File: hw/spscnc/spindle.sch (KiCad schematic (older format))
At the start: 33 parts, among them J1 8P8C_4xShielded, J2 8P8C_4xShielded, J3 Conn_01x04_Female, Q1 KIA50N06B, Q2 KIA50N06B, Q3 KIA50N06B, Q4 KIA50N06B, U1 IR2104, U2 IR2104

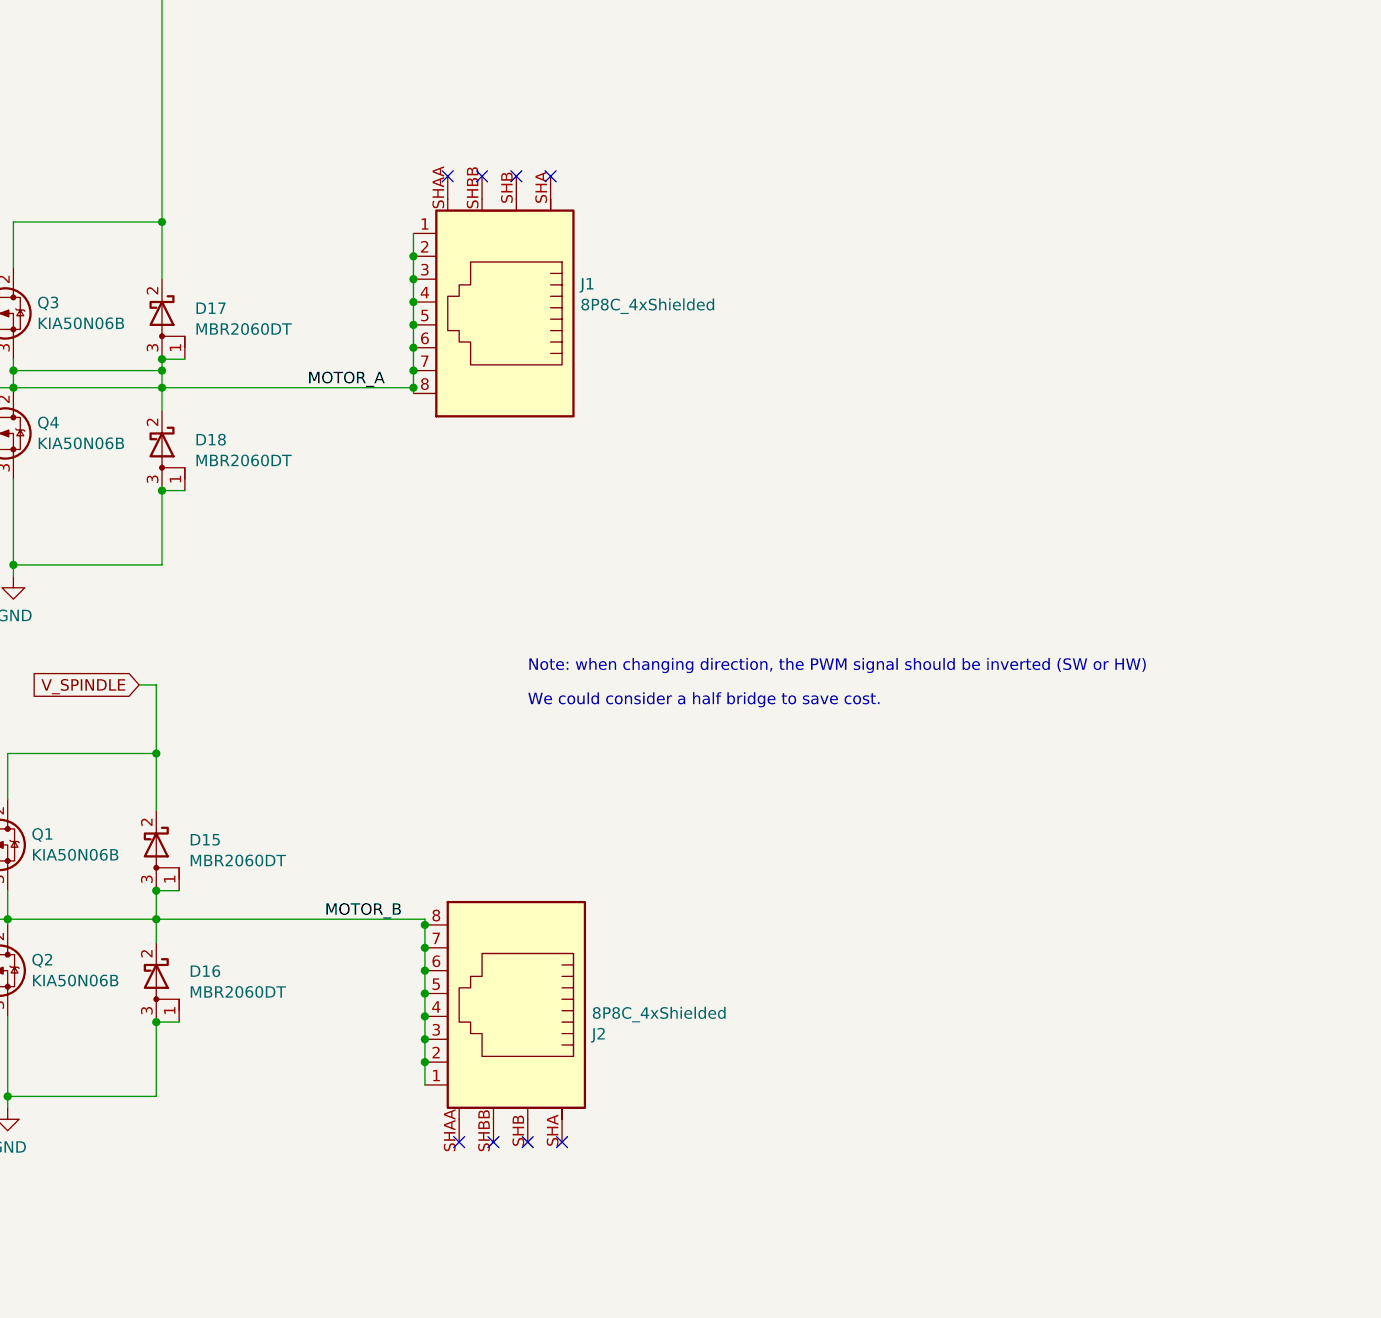
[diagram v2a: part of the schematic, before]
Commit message: added most corrections on the schematic for i2s operation.
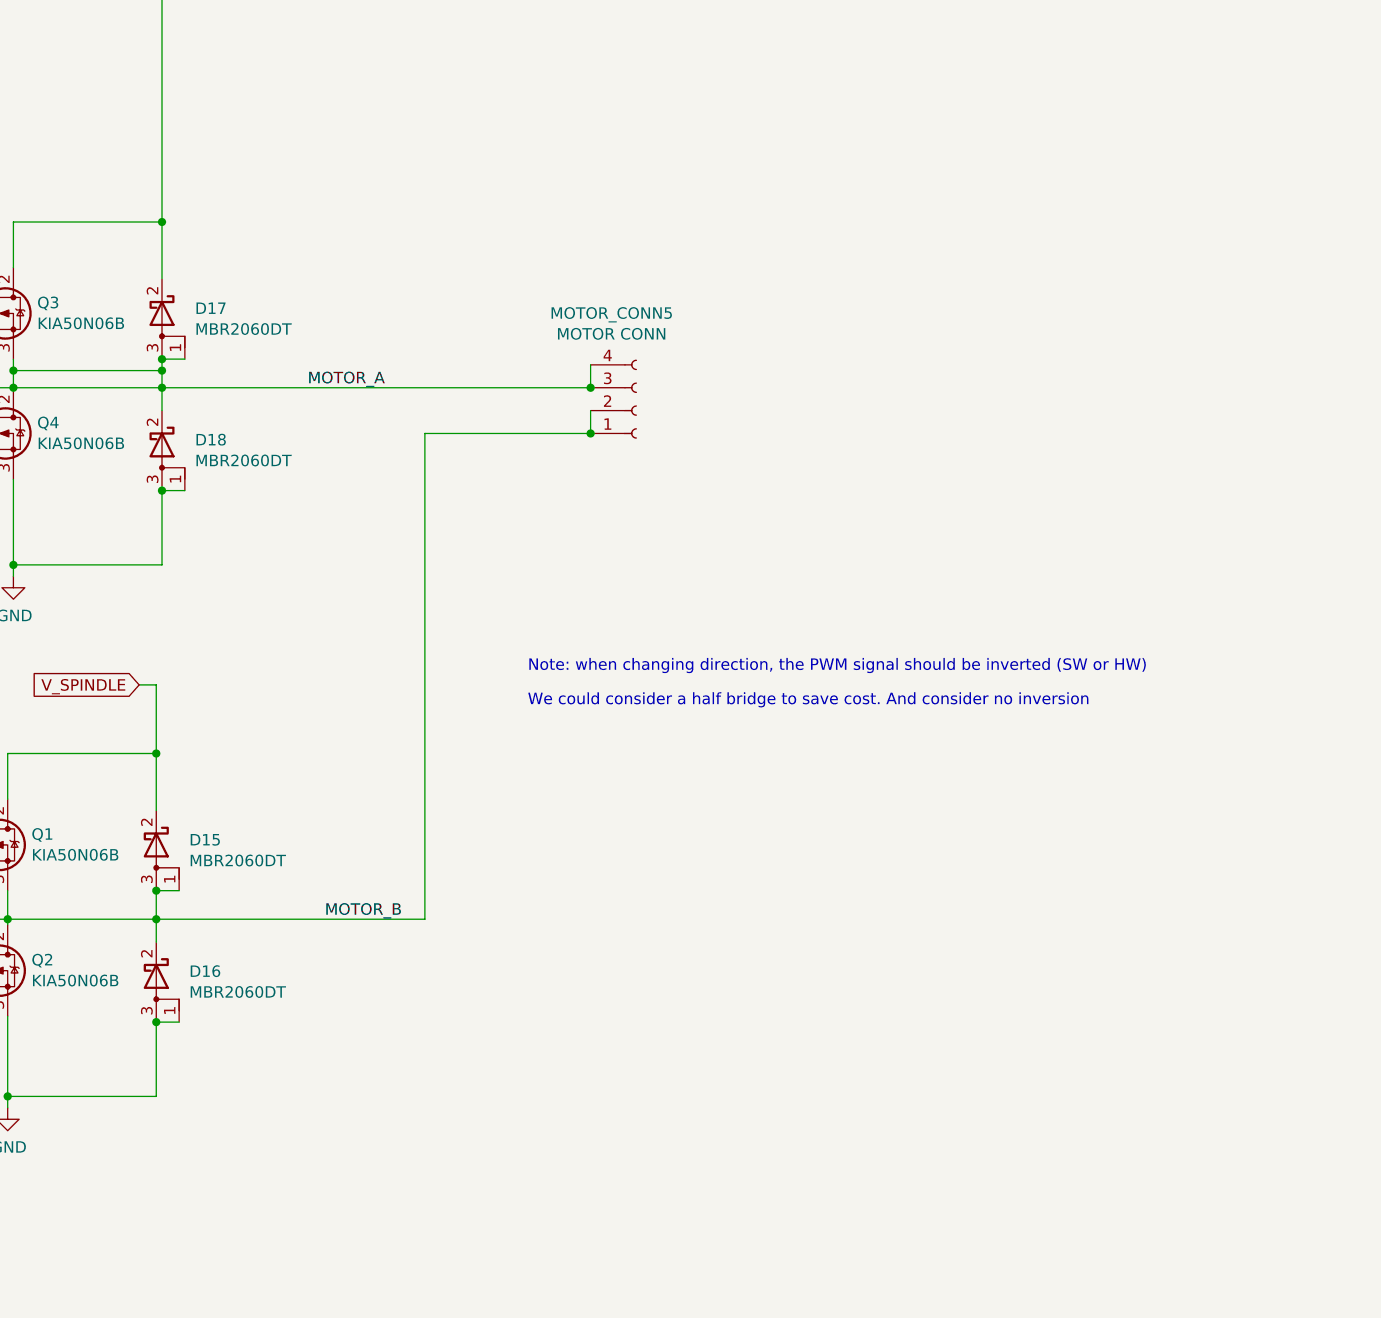
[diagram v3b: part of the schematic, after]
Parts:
- removed J1, J2: 8P8C_4xShielded, industrial000:rj45_R-RJ45S08P-B000_C386763, symbol industrial:8P8C_4xShielded
- added MOTOR_CONN5: MOTOR CONN, Connector_Phoenix_MSTB:PhoenixContact_MSTBV_2,5_4-GF-5,08_1x04_P5.08mm_Vertical_ThreadedFlange_MountHole, symbol Connector:Conn_01x04_Female
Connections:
- net MOTOR_A: now also MOTOR_CONN5.3 (Pin_3), MOTOR_CONN5.4 (Pin_4)
- net MOTOR_B: now also MOTOR_CONN5.1 (Pin_1), MOTOR_CONN5.2 (Pin_2)
- no-connect marks 8 -> 0
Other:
- note added: "We could consider a half bridge to save cost. And consider no inversion"
- note removed: "We could consider a half bridge to save cost."
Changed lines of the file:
@@
 $Descr A4 11693 8268
 encoding utf-8
-Sheet 5 16
+Sheet 5 17
 Title "Trinamic FluidNC CNC Controller"
 Date "2022-01-27"
@@
 Text HLabel 3575 2475 0    50   Input ~ 0
 PWM_IN
-NoConn ~ 7175 1750
-NoConn ~ 7325 1750
-NoConn ~ 7475 1750
-NoConn ~ 7625 1750
-NoConn ~ 7675 5975
-NoConn ~ 7525 5975
-NoConn ~ 7375 5975
-NoConn ~ 7225 5975
 Text Label 6900 2675 2    50   ~ 0
 MOTOR_A
-Wire Wire Line
-	7025 2700 7025 2675
-Connection ~ 7025 2600
-Wire Wire Line
-	7025 2600 7025 2500
-Connection ~ 7025 2500
-Wire Wire Line
-	7025 2500 7025 2400
-Connection ~ 7025 2400
-Wire Wire Line
-	7025 2400 7025 2300
-Connection ~ 7025 2300
-Wire Wire Line
-	7025 2300 7025 2200
-Connection ~ 7025 2200
-Wire Wire Line
-	7025 2200 7025 2100
-Connection ~ 7025 2100
-Wire Wire Line
-	7025 2100 7025 2000
-Wire Wire Line
-	7075 5725 7075 5625
-Connection ~ 7075 5025
-Connection ~ 7075 5125
-Wire Wire Line
-	7075 5125 7075 5025
-Connection ~ 7075 5225
-Wire Wire Line
-	7075 5225 7075 5125
-Connection ~ 7075 5325
-Wire Wire Line
-	7075 5325 7075 5225
-Connection ~ 7075 5425
-Wire Wire Line
-	7075 5425 7075 5325
-Connection ~ 7075 5525
-Wire Wire Line
-	7075 5525 7075 5425
-Connection ~ 7075 5625
-Wire Wire Line
-	7075 5625 7075 5525
 Text Label 6975 5000 2    50   ~ 0
 MOTOR_B
@@
 Wire Wire Line
 	5275 2675 5925 2675
-Connection ~ 7025 2675
-Wire Wire Line
-	7025 2675 7025 2600
 Connection ~ 5925 2675
 Wire Wire Line
 	5925 2675 5925 2600
 Wire Wire Line
-	5925 2675 7025 2675
-Wire Wire Line
 	5925 2675 5925 2775
 Wire Wire Line
 	5900 5000 7075 5000
-Wire Wire Line
-	7075 5000 7075 5025
 Wire Wire Line
 	5900 5000 5900 5100
@@
 Wire Wire Line
 	2725 1600 2725 1575
-$Comp
-L industrial:8P8C_4xShielded J?
-U 1 1 61D212C1
-P 7425 2300
-AR Path="/61C80DFB/61D212C1" Ref="J?"  Part="1"
-AR Path="/61C80E48/61D212C1" Ref="J?"  Part="1"
-AR Path="/61C80E8F/61D212C1" Ref="J?"  Part="1"
-AR Path="/61CEF4C9/61D212C1" Ref="J?"  Part="1"
-AR Path="/61C80DCB/61D212C1" Ref="J1"  Part="1"
-F 0 "J1" H 7095 2222 50  0000 R CNN
-F 1 "8P8C_4xShielded" H 7095 2313 50  0000 R CNN
-F 2 "industrial000:rj45_R-RJ45S08P-B000_C386763" V 7425 2325 50  0001 C CNN
-F 3 "~" V 7425 2325 50  0001 C CNN
-F 4 "DNP007" H 7425 2300 50  0001 C CNN "jlcpcb"
-	1    7425 2300
-	-1   0    0    1
-$EndComp
-$Comp
-L industrial:8P8C_4xShielded J?
-U 1 1 61D219D4
-P 7475 5425
-AR Path="/61C80DFB/61D219D4" Ref="J?"  Part="1"
-AR Path="/61C80E48/61D219D4" Ref="J?"  Part="1"
-AR Path="/61C80E8F/61D219D4" Ref="J?"  Part="1"
-AR Path="/61CEF4C9/61D219D4" Ref="J?"  Part="1"
-AR Path="/61C80DCB/61D219D4" Ref="J2"  Part="1"
-F 0 "J2" H 7145 5347 50  0000 R CNN
-F 1 "8P8C_4xShielded" H 7145 5438 50  0000 R CNN
-F 2 "industrial000:rj45_R-RJ45S08P-B000_C386763" V 7475 5450 50  0001 C CNN
-F 3 "~" V 7475 5450 50  0001 C CNN
-F 4 "DNP007" H 7475 5425 50  0001 C CNN "jlcpcb"
-	1    7475 5425
-	-1   0    0    -1
-$EndComp
 $Comp
 L Driver_FET:IR2104 U2
@@
 $EndComp
 Text Notes 7525 4075 0    50   ~ 0
-We could consider a half bridge to save cost.
+We could consider a half bridge to save cost. And consider no inversion
 $Comp
 L Device:R R150
@@
 Wire Wire Line
 	1475 6025 2200 6025
+$Comp
+L Connector:Conn_01x04_Female MOTOR_CONN?
+U 1 1 623B8ED3
+P 8000 2775
+AR Path="/61E0961E/623B8ED3" Ref="MOTOR_CONN?"  Part="1"
+AR Path="/61C743E7/61AF0AE8/623B8ED3" Ref="MOTOR_CONN?"  Part="1"
+AR Path="/61E601B6/623B8ED3" Ref="MOTOR_CONN?"  Part="1"
+AR Path="/6203D74D/623B8ED3" Ref="MOTOR_CONN?"  Part="1"
+AR Path="/6203DA5D/623B8ED3" Ref="MOTOR_CONN?"  Part="1"
+AR Path="/6203DFCF/623B8ED3" Ref="MOTOR_CONN?"  Part="1"
+AR Path="/6221509B/623B8ED3" Ref="MOTOR_CONN?"  Part="1"
+AR Path="/61C80DCB/623B8ED3" Ref="MOTOR_CONN5"  Part="1"
+F 0 "MOTOR_CONN5" H 7892 2350 50  0000 C CNN
+F 1 "MOTOR CONN" H 7892 2441 50  0000 C CNN
+F 2 "Connector_Phoenix_MSTB:PhoenixContact_MSTBV_2,5_4-GF-5,08_1x04_P5.08mm_Vertical_ThreadedFlange_MountHole" H 8000 2775 50  0001 C CNN
+F 3 "~" H 8000 2775 50  0001 C CNN
+F 4 "DNP006" H 8000 2775 50  0001 C CNN "jlcpcb"
+	1    8000 2775
+	1    0    0    1
+$EndComp
+Wire Wire Line
+	7800 2675 7800 2575
+Connection ~ 7800 2675
+Wire Wire Line
+	5925 2675 7800 2675
+Wire Wire Line
+	7800 2875 7800 2775
+Wire Wire Line
+	7800 2875 7075 2875
+Wire Wire Line
+	7075 2875 7075 5000
+Connection ~ 7800 2875
 $EndSCHEMATC

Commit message: Finished preliminary routing, pending checklist and review
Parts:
- removed C10: 330uF @60V, Capacitor_THT:CP_Radial_D24.0mm_P10.00mm_SnapIn, symbol Device:CP
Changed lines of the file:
@@
 	1525 1000 1525 875
 Connection ~ 1525 875
-Wire Wire Line
-	1525 875  1750 875
 $Comp
 L power:GND-power #PWR01
@@
 Wire Wire Line
 	1525 1425 1525 1300
-Wire Wire Line
-	1525 1300 1750 1300
 Connection ~ 1525 1300
-Connection ~ 1750 1300
-Wire Wire Line
-	1750 1300 2175 1300
 Wire Wire Line
 	2175 1000 2175 875
@@
 Wire Wire Line
 	2175 875  5925 875
-Wire Wire Line
-	1750 1000 1750 875
-Connection ~ 1750 875
-Wire Wire Line
-	1750 875  2175 875
 Wire Wire Line
 	2950 1600 2725 1600
@@
 	1    5900 5250
 	0    1    1    0
-$EndComp
-$Comp
-L Device:CP C10
-U 1 1 61E7AF08
-P 1750 1150
-F 0 "C10" H 1775 1250 50  0000 L CNN
-F 1 "330uF @60V" H 1750 900 50  0000 L CNN
-F 2 "Capacitor_THT:CP_Radial_D24.0mm_P10.00mm_SnapIn" H 1788 1000 50  0001 C CNN
-F 3 "~" H 1750 1150 50  0001 C CNN
-F 4 "DNP015" H 1750 1150 50  0001 C CNN "jlcpcb"
-	1    1750 1150
-	1    0    0    -1
 $EndComp
 $Comp
@@
 	7075 2875 7075 5000
 Connection ~ 7800 2875
+Wire Wire Line
+	1525 1300 2175 1300
+Wire Wire Line
+	1525 875  2175 875
 $EndSCHEMATC

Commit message: As ordered 1.0.1
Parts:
- added JP9: Jumper_NO_Small, Connector_PinHeader_2.54mm:PinHeader_1x02_P2.54mm_Vertical, symbol Device:Jumper_NO_Small
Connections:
- net PWM_IN: now also JP9.1; no longer U2.2 (IN)
- new net: JP9.2, U2.2 (IN)
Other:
- moved on the sheet: C84
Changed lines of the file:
@@
 Sheet 5 17
 Title "Trinamic FluidNC CNC Controller"
-Date "2022-01-27"
-Rev "1.0.0"
+Date "2022-02-12"
+Rev "1.0.1"
 Comp ""
 Comment1 ""
@@
 Text HLabel 3575 2575 0    50   Input ~ 0
 EN
-Text HLabel 3575 2475 0    50   Input ~ 0
+Text HLabel 2900 2475 0    50   Input ~ 0
 PWM_IN
 Text Label 6900 2675 2    50   ~ 0
@@
 L power:GND-power #PWR0141
 U 1 1 61F8E60A
-P 2725 2500
+P 1300 2575
 AR Path="/61F8E60A" Ref="#PWR0141"  Part="1"
 AR Path="/61C80DCB/61F8E60A" Ref="#PWR0141"  Part="1"
-F 0 "#PWR0141" H 2725 2250 50  0001 C CNN
-F 1 "GND" H 2730 2327 50  0000 C CNN
-F 2 "" H 2725 2500 50  0001 C CNN
-F 3 "" H 2725 2500 50  0001 C CNN
-	1    2725 2500
+F 0 "#PWR0141" H 1300 2325 50  0001 C CNN
+F 1 "GND" H 1305 2402 50  0000 C CNN
+F 2 "" H 1300 2575 50  0001 C CNN
+F 3 "" H 1300 2575 50  0001 C CNN
+	1    1300 2575
 	1    0    0    -1
 $EndComp
@@
 L Device:C_Small C?
 U 1 1 61F99538
-P 2725 2400
+P 1300 2475
 AR Path="/61E601B6/61F99538" Ref="C?"  Part="1"
 AR Path="/6203D74D/61F99538" Ref="C?"  Part="1"
@@
 AR Path="/6203DFCF/61F99538" Ref="C?"  Part="1"
 AR Path="/61C80DCB/61F99538" Ref="C84"  Part="1"
-F 0 "C84" V 2496 2400 50  0000 C CNN
-F 1 "100nF" V 2587 2400 50  0000 C CNN
-F 2 "Capacitor_SMD:C_0603_1608Metric" H 2725 2400 50  0001 C CNN
-F 3 "~" H 2725 2400 50  0001 C CNN
-F 4 "C14663" H 2725 2400 50  0001 C CNN "jlcpcb"
-	1    2725 2400
+F 0 "C84" V 1071 2475 50  0000 C CNN
+F 1 "100nF" V 1162 2475 50  0000 C CNN
+F 2 "Capacitor_SMD:C_0603_1608Metric" H 1300 2475 50  0001 C CNN
+F 3 "~" H 1300 2475 50  0001 C CNN
+F 4 "C14663" H 1300 2475 50  0001 C CNN "jlcpcb"
+	1    1300 2475
 	1    0    0    -1
 $EndComp
@@
 L industrial:+5V #PWR0159
 U 1 1 61FB8C06
-P 2725 2300
-F 0 "#PWR0159" H 2725 2150 50  0001 C CNN
-F 1 "+5V" H 2740 2473 50  0000 C CNN
-F 2 "" H 2725 2300 50  0001 C CNN
-F 3 "" H 2725 2300 50  0001 C CNN
-	1    2725 2300
+P 1300 2375
+F 0 "#PWR0159" H 1300 2225 50  0001 C CNN
+F 1 "+5V" H 1315 2548 50  0000 C CNN
+F 2 "" H 1300 2375 50  0001 C CNN
+F 3 "" H 1300 2375 50  0001 C CNN
+	1    1300 2375
 	1    0    0    -1
 $EndComp
@@
 Wire Wire Line
 	1525 875  2175 875
+$Comp
+L Device:Jumper_NO_Small JP9
+U 1 1 620AC53F
+P 3075 2475
+F 0 "JP9" H 3075 2660 50  0000 C CNN
+F 1 "Jumper_NO_Small" H 3075 2569 50  0000 C CNN
+F 2 "Connector_PinHeader_2.54mm:PinHeader_1x02_P2.54mm_Vertical" H 3075 2475 50  0001 C CNN
+F 3 "~" H 3075 2475 50  0001 C CNN
+F 4 "DNP443" H 3075 2475 50  0001 C CNN "jlcpcb"
+	1    3075 2475
+	1    0    0    -1
+$EndComp
+Wire Wire Line
+	2975 2475 2900 2475
+Wire Wire Line
+	3175 2475 3575 2475
 $EndSCHEMATC
